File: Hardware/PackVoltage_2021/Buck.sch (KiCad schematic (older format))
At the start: 14 parts, among them J3V1 Test_Point, J5V1 Test_Point, U12 OKI-78SR-3.3_1.5-W36-C, U13 OKI-78SR-5_1.5-W36-C

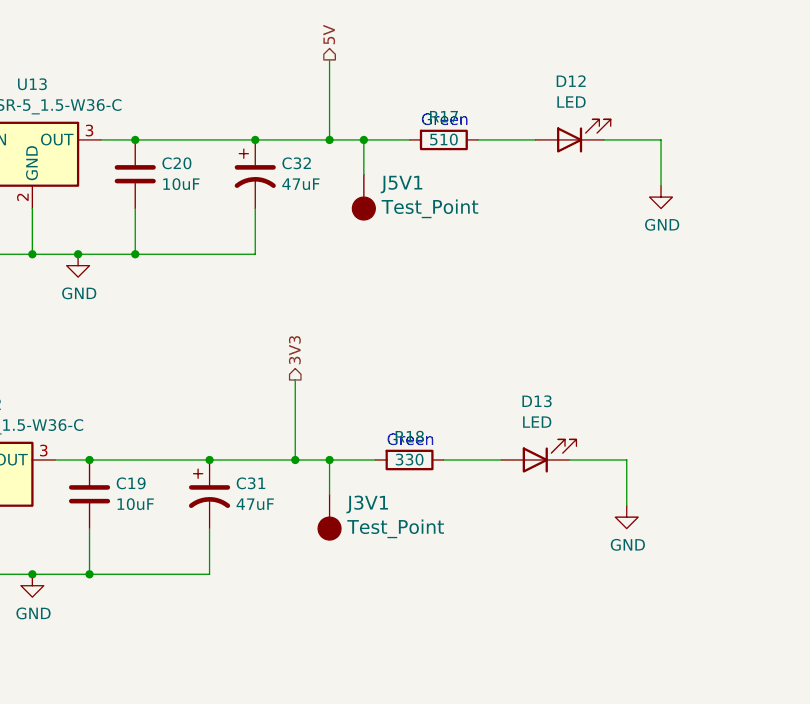
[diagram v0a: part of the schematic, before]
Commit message: circuit, deletes
made circuit to copy across board (hopefully);
deleted old traces that "aren't wide enough"
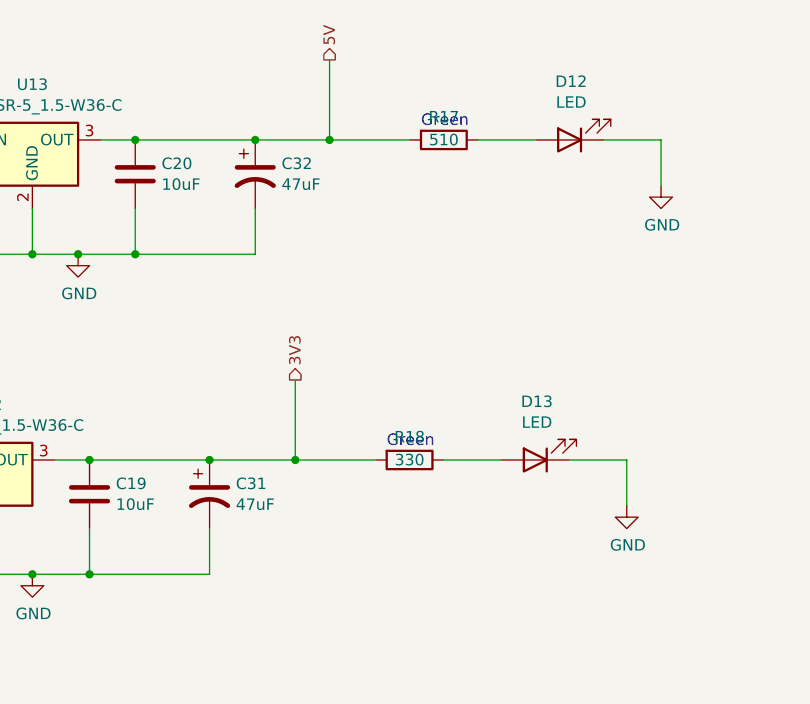
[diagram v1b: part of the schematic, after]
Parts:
- removed J3V1, J5V1: Test_Point, TestPoint:TestPoint_Pad_2.5x2.5mm, symbol PackVoltage_2021_Rev1-rescue:Test_Point-MRDT_Connectors
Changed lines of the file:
@@
 	3425 2975 3425 2625
-$Comp
-L PackVoltage_2021_Rev1-rescue:Test_Point-MRDT_Connectors J5V1
-U 1 1 5F86ADCC
-P 3575 3125
-F 0 "J5V1" H 3497 3164 60  0000 R CNN
-F 1 "Test_Point" H 3497 3270 60  0000 R CNN
-F 2 "TestPoint:TestPoint_Pad_2.5x2.5mm" H 3575 3075 60  0001 C CNN
-F 3 "" H 3575 3075 60  0001 C CNN
-	1    3575 3125
-	-1   0    0    1
-$EndComp
-Wire Wire Line
-	3425 2975 3575 2975
-Wire Wire Line
-	3575 2975 3575 3125
 $Comp
 L Device:LED D12
@@
 $EndComp
 Wire Wire Line
-	3575 2975 3775 2975
-Connection ~ 3575 2975
-Wire Wire Line
 	4075 2975 4325 2975
 Wire Wire Line
@@
 Text Notes 3825 2925 0    50   ~ 0
 Green
-$Comp
-L PackVoltage_2021_Rev1-rescue:Test_Point-MRDT_Connectors J3V1
-U 1 1 5F875043
-P 3425 4525
-F 0 "J3V1" H 3347 4564 60  0000 R CNN
-F 1 "Test_Point" H 3347 4670 60  0000 R CNN
-F 2 "TestPoint:TestPoint_Pad_2.5x2.5mm" H 3425 4475 60  0001 C CNN
-F 3 "" H 3425 4475 60  0001 C CNN
-	1    3425 4525
-	-1   0    0    1
-$EndComp
-Wire Wire Line
-	3275 4375 3425 4375
-Wire Wire Line
-	3425 4375 3425 4525
 $Comp
 L Device:LED D13
@@
 $EndComp
 Wire Wire Line
-	3425 4375 3625 4375
-Connection ~ 3425 4375
-Wire Wire Line
 	3925 4375 4175 4375
 Wire Wire Line
@@
 	1    0    0    -1
 $EndComp
+Wire Wire Line
+	3425 2975 3775 2975
+Wire Wire Line
+	3275 4375 3625 4375
 $EndSCHEMATC
